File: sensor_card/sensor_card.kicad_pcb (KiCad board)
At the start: 2 copper layers, 9 parts, among them J1 Raspberry_Pi_4, J2 BME280, J3 GPS, J4 PARACHUTE, J5 HMI, J6 power LORA, J7 power_RPI, J8 MPU_6500, U1 Ai-Thinker-Ra-02

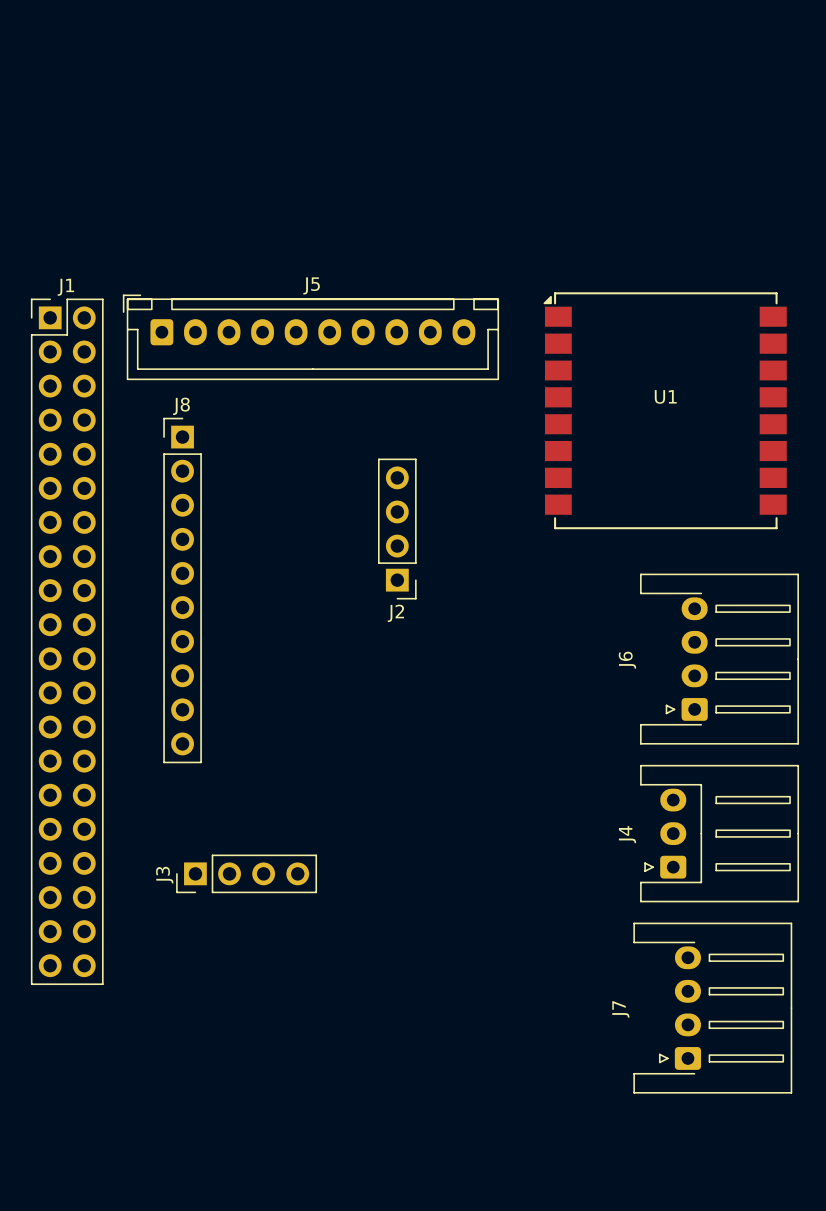
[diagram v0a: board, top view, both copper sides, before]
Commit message: Board Routed Prototype 1 .  Power Routes to be redone
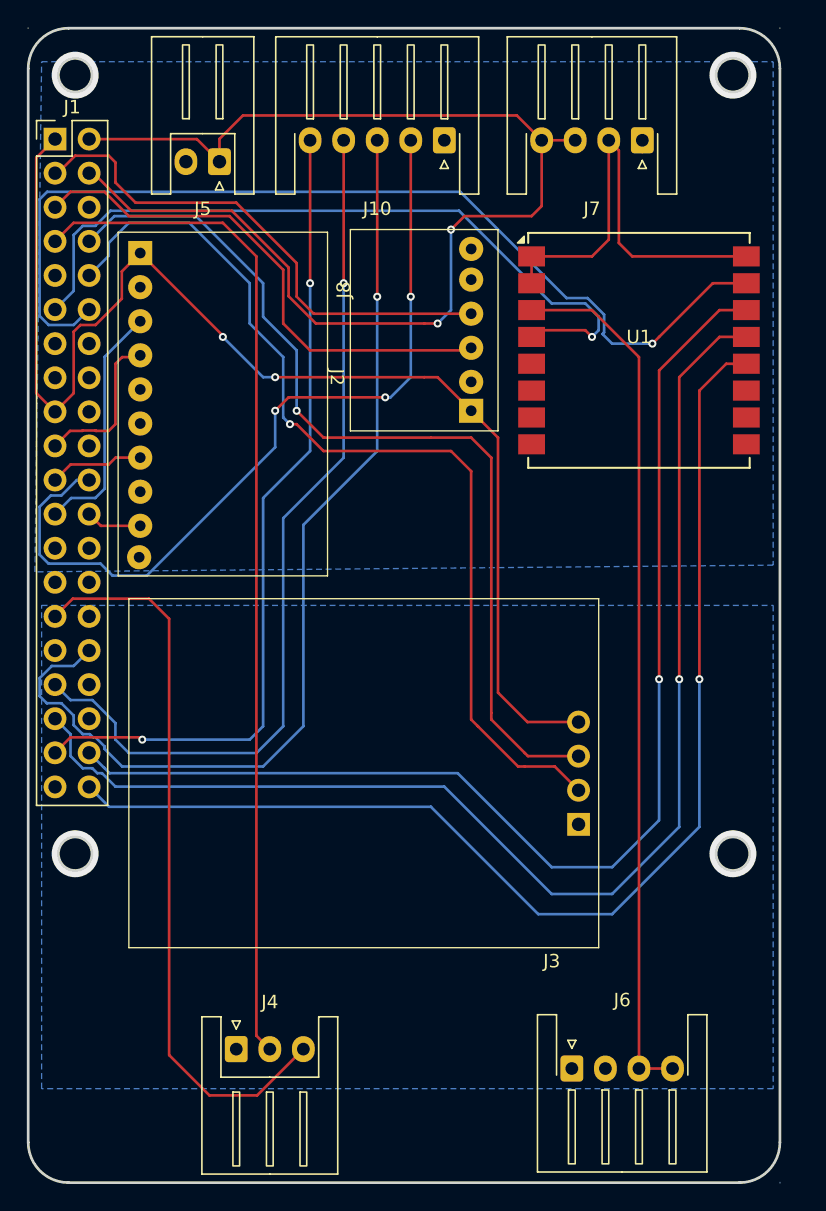
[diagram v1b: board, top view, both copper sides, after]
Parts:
- added J10: Conn_01x05, Connector_JST:JST_XH_S5B-XH-A-1_1x05_P2.50mm_Horizontal, F.Cu at (110.0, 46.4)
- J2: footprint Connector_PinHeader_2.54mm:PinHeader_1x04_P2.54mm_Vertical -> PHOENIX:BME 280
- J3: footprint Connector_PinHeader_2.54mm:PinHeader_1x04_P2.54mm_Vertical -> PHOENIX:GPS-MV2
- J5: value HMI -> Conn_01x02; footprint Connector_JST:JST_XH_B10B-XH-A_1x10_P2.50mm_Vertical -> Connector_JST:JST_XH_S2B-XH-A_1x02_P2.50mm_Horizontal
- J8: footprint Connector_PinHeader_2.54mm:PinHeader_1x10_P2.54mm_Vertical -> PHOENIX:MPU-9250
- moved J7 68.5 mm to (124.8, 46.4), turned to 180 degrees
- moved J4 35.3 mm to (94.5, 114.1), turned to 0 degrees
- moved J6 28.3 mm to (119.5, 115.5), turned to 0 degrees
- moved J2 21.2 mm to (108.0, 58.0), turned to -90 degrees
- moved J3 14.6 mm to (104.0, 93.5), turned to 0 degrees
- moved J5 13.4 mm to (93.2, 47.9), turned to 180 degrees
- moved J1 13.3 mm to (81.0, 46.3)
- moved U1 4.92 mm to (124.5, 62.0)
- moved J8 4.21 mm to (93.5, 65.5), turned to 90 degrees
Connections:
- J4 pad 2: /PARA_STATE_FEEDBACK -> /PARACHUTE_ACTIVATION
- J4 pad 3: /PARACHUTE_ACTIVATION -> /PARA_STATE_FEEDBACK
- J5 pad 1: GND -> +5V
- J5 pad 2: /LED_ALIM_PARA -> GND
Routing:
- net +3V3: track 0.00 -> 94.9 mm, vias 0 -> 2
- net /LORA_MISO: track 0.00 -> 94.7 mm, vias 0 -> 1
- net +5V: track 0.00 -> 91.7 mm, vias 0 -> 2
- net /LORA_MOSI: track 0.00 -> 89.3 mm, vias 0 -> 1
- net /LORA_SCK: track 0.00 -> 88.9 mm, vias 0 -> 1
- net /PARACHUTE_ACTIVATION: track 0.00 -> 76.1 mm
- net /LED_ALIM_LORA: track 0.00 -> 75.4 mm, vias 0 -> 1
- net /LORA_CS: track 0.00 -> 73.6 mm, vias 0 -> 1
- net /GPS_TX: track 0.00 -> 71.4 mm, vias 0 -> 1
- net /GPS_RX: track 0.00 -> 69.4 mm, vias 0 -> 1
- net /LED_FONC_LORA: track 0.00 -> 66.2 mm, vias 0 -> 1
- net +3V3_LORA: track 0.00 -> 64.9 mm
- net /LED_ALIM_RPI_CAPTEURS: track 0.00 -> 61.7 mm, vias 0 -> 3
- net /LED_FONC_PROGRAMMES: track 0.00 -> 61.6 mm, vias 0 -> 2
- net /LORA_RST: track 0.00 -> 55.9 mm, vias 0 -> 1
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- added copper zone on B.Cu, net GND
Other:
- board outline added: 56 x 86 mm

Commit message: Fully Routed Sensor board
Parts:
- added H1: MountingHole_RPI, MountingHole:MountingHole_2.2mm_M2_DIN965_Pad, F.Cu at (82.5, 41.5)
- added H2: MountingHole_Pad, MountingHole:MountingHole_3.2mm_M3_DIN965_Pad, F.Cu at (75.0, 42.3)
- added H3: MountingHole_Pad, MountingHole:MountingHole_3.2mm_M3_DIN965_Pad, F.Cu at (139.0, 42.3)
- added H4: MountingHole_Pad, MountingHole:MountingHole_3.2mm_M3_DIN965_Pad, F.Cu at (75.0, 119.3)
- added H5: MountingHole_Pad, MountingHole:MountingHole_3.2mm_M3_DIN965_Pad, F.Cu at (139.0, 119.3)
- added H6: MountingHole_RPI, MountingHole:MountingHole_2.2mm_M2_DIN965_Pad, F.Cu at (131.5, 41.5)
- added H7: MountingHole_RPI, MountingHole:MountingHole_2.2mm_M2_DIN965_Pad, F.Cu at (131.5, 99.5)
- added H8: MountingHole_RPI, MountingHole:MountingHole_2.2mm_M2_DIN965_Pad, F.Cu at (82.5, 99.5)
- J1: footprint Connector_PinHeader_2.54mm:PinHeader_2x20_P2.54mm_Vertical -> Connector_PinSocket_2.54mm:PinSocket_2x20_P2.54mm_Vertical; moved to B.Cu
- moved J1 49.4 mm to (130.4, 46.4), turned to 180 degrees
- moved J2 5.94 mm to (102.1, 58.7)
- moved J8 5.94 mm to (87.6, 66.2)
- moved U1 5.94 mm to (118.6, 62.7)
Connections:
- J1 pad 15: /LED_ALIM_PARA -> unconnected-(J1-GPIO22/SDIO_CLK-Pad15)
- J1 pad 16: /LED_OUVERT_PARA -> unconnected-(J1-GPIO23/SDIO_CMD-Pad16)
- J1 pad 18: /LED_DECL_PARA -> unconnected-(J1-GPIO24/SDIO_DAT0-Pad18)
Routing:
- net /MPU_MISO: track 7.04 -> 79.7 mm, vias 0 -> 1
- net /LORA_CS: track 73.6 -> 6.93 mm, vias 1 -> 0
- net /MPU_MOSI: track 11.8 -> 74.0 mm, vias 0 -> 1
- net /MPU_CS: track 4.17 -> 64.5 mm, vias 0 -> 1
- net /LORA_MOSI: track 89.3 -> 36.9 mm, vias 1 -> 0
- net /LORA_SCK: track 88.9 -> 37.2 mm, vias 1 -> 0
- net /LORA_MISO: track 94.7 -> 43.1 mm, vias 1 -> 0
- net +3V3: track 94.9 -> 146.1 mm, vias 2 -> 1
- net +5V: track 91.7 -> 50.9 mm, vias 2 -> 0
- net /MPU_SCK: track 18.1 -> 54.7 mm
- net /PARACHUTE_ACTIVATION: track 76.1 -> 106.6 mm
- net /PARA_STATE_FEEDBACK: track 54.8 -> 77.5 mm, vias 0 -> 1
- net GND: track 34.4 -> 50.8 mm, vias 0 -> 5
- net /GPS_TX: track 71.4 -> 57.0 mm, vias 1 -> 0
- net /LED_FONC_PROGRAMMES: track 61.6 -> 75.3 mm
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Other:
- board size 56 x 86 mm -> 72.4 x 86 mm
- board text added: "BME280"
- board text added: "FAN_CON"
- board text added: "GPS"
- board text added: "HMI_CON"
- board text added: "LORA"
- board text added: "MPU_6500"
- board text added: "PARACHUTE_CON"
- board text added: "POWER_LORA_CON"
- board text added: "POWER_RPI"
- board text added: "RPI_CON_2x20_FEM"

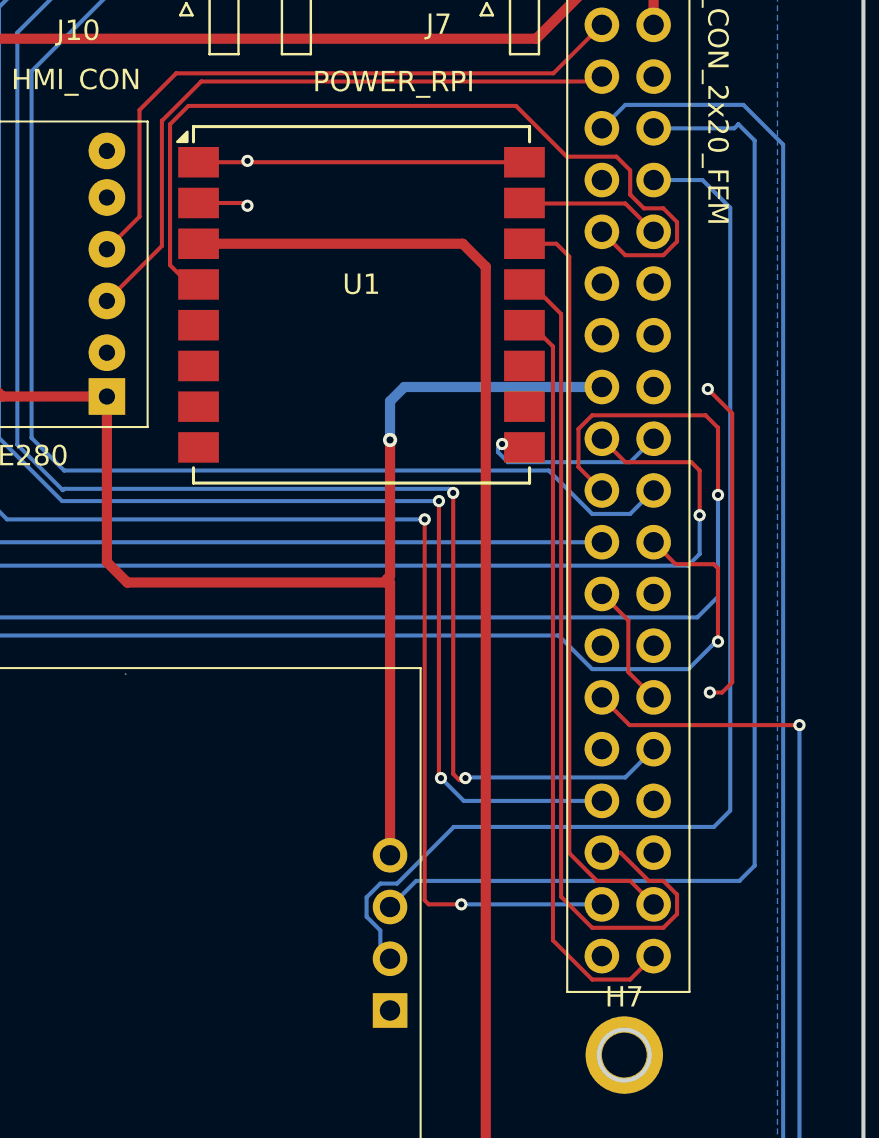
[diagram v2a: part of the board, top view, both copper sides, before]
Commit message: Fully routed power board
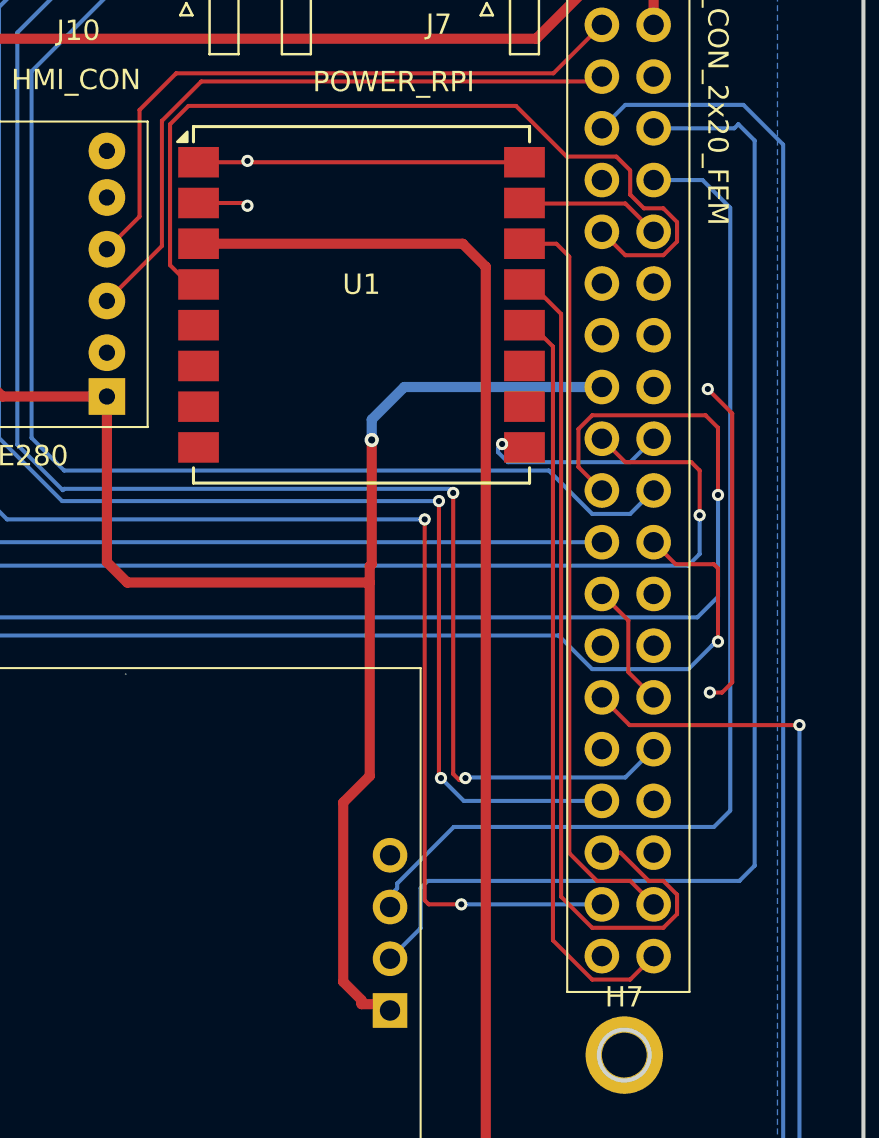
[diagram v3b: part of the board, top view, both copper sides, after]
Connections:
- J3 pad 1: GND -> +3V3
- J3 pad 2: /GPS_TX -> /GPS_RX
- J3 pad 3: /GPS_RX -> /GPS_TX
- J3 pad 4: +3V3 -> GND
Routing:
- net +3V3: track 146.1 -> 155.2 mm
- net /GPS_TX: track 57.0 -> 52.9 mm
- net /GPS_RX: track 59.7 -> 62.6 mm

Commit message: sensor card: full revision
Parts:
- added J11: power LORA, Connector_JST:JST_XH_S4B-XH-A_1x04_P2.50mm_Horizontal, F.Cu at (148.8, 120.0)
- added J12: AIRBRAKE, Connector_JST:JST_XH_S4B-XH-A_1x04_P2.50mm_Horizontal, F.Cu at (170.0, 54.0)
- added J9: proto_selector, Connector_PinHeader_2.54mm:PinHeader_2x02_P2.54mm_Vertical, F.Cu at (153.4, 53.5)
- added R1: 10k, Resistor_THT:R_Axial_DIN0204_L3.6mm_D1.6mm_P7.62mm_Horizontal, F.Cu at (138.4, 114.3)
- H1: value MountingHole_RPI -> MountingHole_3.2mm_M3; footprint MountingHole:MountingHole_2.2mm_M2_DIN965_Pad -> MountingHole:MountingHole_3.2mm_M3
- H2, H3, H4: value MountingHole_Pad -> MountingHole_3.2mm_M3; footprint MountingHole:MountingHole_3.2mm_M3_DIN965_Pad -> MountingHole:MountingHole_3.2mm_M3
- H5: value MountingHole_Pad -> MountingHole_2.7mm_M2.5; footprint MountingHole:MountingHole_3.2mm_M3_DIN965_Pad -> MountingHole:MountingHole_2.7mm_M2.5
- H6, H7, H8: value MountingHole_RPI -> MountingHole_2.7mm_M2.5; footprint MountingHole:MountingHole_2.2mm_M2_DIN965_Pad -> MountingHole:MountingHole_2.7mm_M2.5
- J1: value Raspberry_Pi_4 -> fan_power; footprint Connector_PinSocket_2.54mm:PinSocket_2x20_P2.54mm_Vertical -> Connector_PinHeader_2.54mm:PinHeader_1x02_P2.54mm_Horizontal
- J10: value Conn_01x05 -> power_RPI; footprint Connector_JST:JST_XH_S5B-XH-A-1_1x05_P2.50mm_Horizontal -> Connector_JST:JST_XH_S4B-XH-A_1x04_P2.50mm_Horizontal
- J2: value BME280 -> BME; footprint PHOENIX:BME 280 -> nasa:BME280
- J3: footprint PHOENIX:GPS-MV2 -> nasa:GPS
- J4: value PARACHUTE -> Raspberry_Pi_4; footprint Connector_JST:JST_XH_S3B-XH-A_1x03_P2.50mm_Horizontal -> Connector_PinSocket_2.54mm:PinSocket_2x20_P2.54mm_Vertical; moved to B.Cu
- J5: value Conn_01x02 -> PARACHUTE; footprint Connector_JST:JST_XH_S2B-XH-A_1x02_P2.50mm_Horizontal -> Connector_JST:JST_XH_S3B-XH-A_1x03_P2.50mm_Horizontal
- J6: value power LORA -> MPU_6500; footprint Connector_JST:JST_XH_S4B-XH-A-1_1x04_P2.50mm_Horizontal -> nasa:MPU6500
- J7: value power_RPI -> hmi; footprint Connector_JST:JST_XH_S4B-XH-A-1_1x04_P2.50mm_Horizontal -> Connector_JST:JST_XH_S5B-XH-A_1x05_P2.50mm_Horizontal
- J8: value MPU_6500 -> lauch; footprint PHOENIX:MPU-9250 -> Connector_JST:JST_XH_S2B-XH-A_1x02_P2.50mm_Horizontal
- U1: moved to B.Cu
- moved H4 120.7 mm to (195.5, 127.0)
- moved H2 120.6 mm to (195.5, 46.5)
- moved J4 109.6 mm to (186.7, 54.9), turned to 180 degrees
- moved H8 105.8 mm to (188.0, 108.0)
- moved J10 101.8 mm to (180.2, 120.0), turned to 0 degrees
- moved J5 88.5 mm to (181.5, 54.0)
- moved H3 85.0 mm to (131.5, 127.0)
- moved J7 83.2 mm to (163.5, 120.0), turned to 0 degrees
- moved J8 74.5 mm to (139.0, 120.1), turned to 0 degrees
- moved H5 69.3 mm to (139.0, 50.0)
- moved H6 57.1 mm to (188.0, 50.0)
- moved H1 49.3 mm to (131.5, 46.5)
- moved J3 40.0 mm to (142.7, 103.5), turned to 90 degrees
- moved J2 35.1 mm to (137.0, 55.2), turned to 0 degrees
- moved J6 28.5 mm to (126.3, 87.8), turned to 90 degrees
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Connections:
- J1 pad 1: +3V3 -> GND
- J10 pad 2: /LED_ALIM_RPI_CAPTEURS -> GND
- J10 pad 3: /LED_ALIM_LORA -> +5V
- J10 pad 4: /LED_FONC_LORA -> +5V
- J2 pad 5: (no net) -> unconnected-(J2-Pin_5-Pad5)
- J2 pad 6: (no net) -> unconnected-(J2-Pin_6-Pad6)
- J3 pad 1: +3V3 -> GND
- J3 pad 2: /GPS_RX -> /GPS_TX
- J3 pad 3: /GPS_TX -> /GPS_RX
- J3 pad 4: GND -> +3V3
- J4 pad 1: GND -> +3V3
- J4 pad 2: /PARACHUTE_ACTIVATION -> +5V
- J4 pad 3: /PARA_STATE_FEEDBACK -> /SDA
- J5 pad 1: +5V -> GND
- J5 pad 2: GND -> /PARACHUTE_ACTIVATION
- J6 pad 1: GND -> +3V3
- J6 pad 3: +3V3_LORA -> /MPU_SCK
- J6 pad 4: +3V3_LORA -> /MPU_MOSI
- J7 pad 2: GND -> +3V3_LORA
- J7 pad 3: +5V -> /LED_LORA_WORKING
- J7 pad 4: +5V -> +3V3
- J8 pad 1: +3V3 -> GND
- J8 pad 2: GND -> /lauch_detect
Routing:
- net /PARACHUTE_ACTIVATION: track 106.6 -> 11.7 mm
- net /PARA_STATE_FEEDBACK: track 77.5 -> 0.00 mm, vias 1 -> 0
- net /LED_FONC_PROGRAMMES: track 75.3 -> 0.00 mm, vias 2 -> 0
- net /lauch_detect: track 0.00 -> 73.8 mm
- net /LED_ALIM_LORA: track 71.8 -> 0.00 mm, vias 2 -> 0
- net +5V: track 50.9 -> 121.4 mm
- net /LED_FONC_LORA: track 68.4 -> 0.00 mm, vias 2 -> 0
- net /AIRBRAKE_RX_SCL: track 0.00 -> 67.9 mm
- net /AIRBRAKE_TX_SDA: track 0.00 -> 67.2 mm
- net /GPS_TX: track 52.9 -> 116.9 mm
- net /MPU_SCK: track 54.7 -> 114.5 mm
- net /LORA_CS: track 6.93 -> 65.1 mm
- net /LED_ALIM_RPI_CAPTEURS: track 57.7 -> 0.00 mm
- net /GPS_RX: track 62.6 -> 120.1 mm
- net /LED_PROG_WORKING: track 0.00 -> 57.2 mm
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- added copper zone on F.Cu, net GND
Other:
- board size 72.4 x 86 mm -> 70 x 86.5 mm
- board text added: "AIRBRAKE"
- board text added: "GND"
- board text added: "HMI"
- board text added: "LAUCH"
- board text added: "PARACHUTE"
- board text added: "PWR-LORA"
- board text added: "PWR-RPI"
- board text removed: "BME280"
- board text removed: "FAN_CON"
- board text removed: "GPS"
- board text removed: "HMI_CON"
- board text removed: "LORA"
- board text removed: "MPU_6500"
- board text removed: "PARACHUTE_CON"
- board text removed: "POWER_LORA_CON"
- board text removed: "POWER_RPI"
- board text removed: "RPI_CON_2x20_FEM"
